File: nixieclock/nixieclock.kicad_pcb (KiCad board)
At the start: 4 copper layers, 96.5 x 92.8 mm, 136 parts, among them J1 USB_C_Receptacle, J2 Conn_ARM_JTAG_SWD_10, Q10 BSS131, Q11 BSS131, Q12 BSS131, Q13 BSS131, Q14 BSS131, Q15 BSS131, Q16 BSS131, Q17 BSS131, Q18 BSS131, Q19 BSS131, Q2 IRLR3110ZTRPBF, Q20 BSS131, Q21 BSS131, Q22 BSS131, Q23 BSS131, Q24 BSS131, Q25 BSS131, Q26 BSS131, Q27 BSS131, Q28 BSS131, Q29 BSS131, Q3 BSR92P, Q30 BSS131, Q31 BSS131, Q32 BSS131, Q33 BSS131, Q34 BSS131, Q35 BSS131, Q36 BSS131, Q37 BSS131, Q38 BSS131, Q39 BSS131, Q4 BSR92P, Q40 BSS131, Q41 BSS131, Q42 BSS131, Q43 BSS131, Q44 BSS131, Q45 BSS131, Q46 BSS131, Q47 BSS131, Q48 BSS131, Q5 BSS131, Q6 BSS131, Q7 BSS131, Q8 BSS131, Q9 BSS131, SW1 EN11-VSM, U1 LT3757AEMSE, U2 AMS1117-3.3, U3 74HC595, U4 74HC595, U5 74HC595, U6 74HC595, U7 74HC595, U8 STM32F051R4Tx, Y1 8MHz, Y2 32.768kHz

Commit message: finalized design ready for quality check
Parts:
- added D2: LTST-C190GKT, LED_SMD:LED_0603_1608Metric_Pad1.05x0.95mm_HandSolder, F.Cu at (113.0, 76.8)
- added D3: LTST-C190GKT, LED_SMD:LED_0603_1608Metric_Pad1.05x0.95mm_HandSolder, F.Cu at (114.8, 76.8)
- added D4: LTST-C190GKT, LED_SMD:LED_0603_1608Metric_Pad1.05x0.95mm_HandSolder, F.Cu at (116.5, 76.8)
- added H1: MountingHole, MountingHole:MountingHole_5.3mm_M5_Pad, F.Cu at (56.0, 76.0)
- added H2: MountingHole, MountingHole:MountingHole_5.3mm_M5_Pad, F.Cu at (56.0, 157.0)
- added H3: MountingHole, MountingHole:MountingHole_5.3mm_M5_Pad, F.Cu at (164.0, 157.0)
- added H4: MountingHole, MountingHole:MountingHole_5.3mm_M5_Pad, F.Cu at (164.0, 76.0)
- added R32: 3.3k, Resistor_SMD:R_0603_1608Metric_Pad1.05x0.95mm_HandSolder, F.Cu at (113.0, 80.2)
- added R33: 1.2k, Resistor_SMD:R_0603_1608Metric_Pad1.05x0.95mm_HandSolder, F.Cu at (114.8, 80.2)
- added R34: 1.2k, Resistor_SMD:R_0603_1608Metric_Pad1.05x0.95mm_HandSolder, F.Cu at (116.5, 80.2)
- added R35: 1M, Resistor_SMD:R_0603_1608Metric_Pad1.05x0.95mm_HandSolder, F.Cu at (72.5, 113.2)
- added R36: 1M, Resistor_SMD:R_0603_1608Metric_Pad1.05x0.95mm_HandSolder, F.Cu at (80.5, 113.2)
- added R37: 1M, Resistor_SMD:R_0603_1608Metric_Pad1.05x0.95mm_HandSolder, F.Cu at (84.5, 113.2)
- added R38: 1M, Resistor_SMD:R_0603_1608Metric_Pad1.05x0.95mm_HandSolder, F.Cu at (84.5, 139.3)
- added R39: 1M, Resistor_SMD:R_0603_1608Metric_Pad1.05x0.95mm_HandSolder, F.Cu at (82.3, 142.3)
- added R40: 1M, Resistor_SMD:R_0603_1608Metric_Pad1.05x0.95mm_HandSolder, F.Cu at (78.5, 146.3)
- added R41: 1M, Resistor_SMD:R_0603_1608Metric_Pad1.05x0.95mm_HandSolder, F.Cu at (74.5, 146.3)
- added R42: 1M, Resistor_SMD:R_0603_1608Metric_Pad1.05x0.95mm_HandSolder, F.Cu at (70.7, 142.3)
- added R43: 1M, Resistor_SMD:R_0603_1608Metric_Pad1.05x0.95mm_HandSolder, F.Cu at (68.5, 139.3)
- added R44: 1M, Resistor_SMD:R_0603_1608Metric_Pad1.05x0.95mm_HandSolder, F.Cu at (68.5, 113.2)
- added R45: 1M, Resistor_SMD:R_0603_1608Metric_Pad1.05x0.95mm_HandSolder, F.Cu at (92.5, 113.2)
- added R46: 1M, Resistor_SMD:R_0603_1608Metric_Pad1.05x0.95mm_HandSolder, F.Cu at (100.5, 113.2)
- added R47: 1M, Resistor_SMD:R_0603_1608Metric_Pad1.05x0.95mm_HandSolder, F.Cu at (104.5, 113.2)
- added R48: 1M, Resistor_SMD:R_0603_1608Metric_Pad1.05x0.95mm_HandSolder, F.Cu at (104.5, 139.3)
- added R49: 1M, Resistor_SMD:R_0603_1608Metric_Pad1.05x0.95mm_HandSolder, F.Cu at (102.3, 142.3)
- added R50: 1M, Resistor_SMD:R_0603_1608Metric_Pad1.05x0.95mm_HandSolder, F.Cu at (98.5, 146.3)
- added R51: 1M, Resistor_SMD:R_0603_1608Metric_Pad1.05x0.95mm_HandSolder, F.Cu at (94.5, 146.3)
- added R52: 1M, Resistor_SMD:R_0603_1608Metric_Pad1.05x0.95mm_HandSolder, F.Cu at (90.7, 142.3)
- added R53: 1M, Resistor_SMD:R_0603_1608Metric_Pad1.05x0.95mm_HandSolder, F.Cu at (88.5, 139.3)
- added R54: 1M, Resistor_SMD:R_0603_1608Metric_Pad1.05x0.95mm_HandSolder, F.Cu at (88.5, 113.2)
- added R55: 1M, Resistor_SMD:R_0603_1608Metric_Pad1.05x0.95mm_HandSolder, F.Cu at (119.5, 113.2)
- added R56: 1M, Resistor_SMD:R_0603_1608Metric_Pad1.05x0.95mm_HandSolder, F.Cu at (127.5, 113.2)
- added R57: 1M, Resistor_SMD:R_0603_1608Metric_Pad1.05x0.95mm_HandSolder, F.Cu at (131.5, 113.2)
- added R58: 1M, Resistor_SMD:R_0603_1608Metric_Pad1.05x0.95mm_HandSolder, F.Cu at (131.5, 139.3)
- added R59: 1M, Resistor_SMD:R_0603_1608Metric_Pad1.05x0.95mm_HandSolder, F.Cu at (129.3, 142.3)
- added R60: 1M, Resistor_SMD:R_0603_1608Metric_Pad1.05x0.95mm_HandSolder, F.Cu at (125.5, 146.3)
- added R61: 1M, Resistor_SMD:R_0603_1608Metric_Pad1.05x0.95mm_HandSolder, F.Cu at (121.5, 146.3)
- added R62: 1M, Resistor_SMD:R_0603_1608Metric_Pad1.05x0.95mm_HandSolder, F.Cu at (117.7, 142.3)
- added R63: 1M, Resistor_SMD:R_0603_1608Metric_Pad1.05x0.95mm_HandSolder, F.Cu at (115.5, 139.3)
- added R64: 1M, Resistor_SMD:R_0603_1608Metric_Pad1.05x0.95mm_HandSolder, F.Cu at (115.5, 113.2)
- added R65: 1M, Resistor_SMD:R_0603_1608Metric_Pad1.05x0.95mm_HandSolder, F.Cu at (139.5, 113.2)
- added R66: 1M, Resistor_SMD:R_0603_1608Metric_Pad1.05x0.95mm_HandSolder, F.Cu at (147.5, 113.2)
- added R67: 1M, Resistor_SMD:R_0603_1608Metric_Pad1.05x0.95mm_HandSolder, F.Cu at (151.5, 113.2)
- added R68: 1M, Resistor_SMD:R_0603_1608Metric_Pad1.05x0.95mm_HandSolder, F.Cu at (151.5, 139.3)
- added R69: 1M, Resistor_SMD:R_0603_1608Metric_Pad1.05x0.95mm_HandSolder, F.Cu at (149.3, 142.3)
- added R70: 1M, Resistor_SMD:R_0603_1608Metric_Pad1.05x0.95mm_HandSolder, F.Cu at (145.5, 146.3)
- added R71: 1M, Resistor_SMD:R_0603_1608Metric_Pad1.05x0.95mm_HandSolder, F.Cu at (141.5, 146.3)
- added R72: 1M, Resistor_SMD:R_0603_1608Metric_Pad1.05x0.95mm_HandSolder, F.Cu at (137.7, 142.3)
- added R73: 1M, Resistor_SMD:R_0603_1608Metric_Pad1.05x0.95mm_HandSolder, F.Cu at (135.5, 139.3)
- added R74: 1M, Resistor_SMD:R_0603_1608Metric_Pad1.05x0.95mm_HandSolder, F.Cu at (135.5, 113.2)
- BT1: footprint Battery:BatteryHolder_Keystone_3000_1x12mm -> Battery:BatteryHolder_MPD_BK912-1x2032
- R21, R22, R23, R24: value 10k -> ?
- R3: value 140k -> 10k
- moved G2 11.2 mm to (122.5, 92.2)
- moved R30 9.63 mm to (146.4, 81.5), turned to 180 degrees
- moved R31 9.19 mm to (144.2, 79.8), turned to 180 degrees
- moved C29 8.54 mm to (155.2, 83.2)
- moved C31 7.37 mm to (144.2, 83.2)
- moved R29 6.96 mm to (153.1, 81.5), turned to 180 degrees
- moved BT1 5.36 mm to (128.6, 79.8)
- moved R19 3.09 mm to (155.2, 79.8), turned to 180 degrees
- moved R20 2.51 mm to (149.8, 83.0)
- moved C30 1.87 mm to (149.8, 80.0)
- moved C1 1.25 mm to (78.5, 86.2)
- moved C10 1.25 mm to (68.2, 85.7)
- moved C11 1.25 mm to (72.0, 82.8)
- moved C12 1.25 mm to (73.5, 82.8)
- moved C13 1.25 mm to (98.0, 79.2)
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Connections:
- R3 pad 1: +3V3 -> GND
- SW1 pad A: (no net) -> Net-(R19-Pad2)
- SW1 pad B: (no net) -> Net-(R30-Pad2)
- U8 pad 37: (no net) -> /microcontroller/ENC_A
- U8 pad 38: (no net) -> /microcontroller/ENC_B
- U8 pad 39: (no net) -> /microcontroller/ENC_SW
- U8 pad 50: (no net) -> Net-(D4-Pad2)
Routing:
- net GND: track 222.3 -> 267.3 mm, vias 208 -> 158
- net Net-(D4-Pad2): track 0.00 -> 30.2 mm
- net /microcontroller/VBAT: track 50.0 -> 71.9 mm
- net VCC: track 16.8 -> 34.3 mm, vias 5 -> 7
- net /microcontroller/ENC_SW: track 0.00 -> 16.9 mm, vias 0 -> 2
- net +3V3: track 33.0 -> 49.5 mm, vias 21 -> 23
- net /cathode_registers/GB0: track 48.0 -> 64.2 mm
- net /microcontroller/ENC_A: track 0.00 -> 11.3 mm
- net Net-(R30-Pad2): track 0.00 -> 9.80 mm
- net Net-(R19-Pad2): track 0.00 -> 9.80 mm
- net /cathode_registers/GB8: track 39.2 -> 30.4 mm
- net /microcontroller/ENC_B: track 0.00 -> 7.62 mm
- net /cathode_registers/LCLK: track 179.5 -> 175.1 mm
- net /cathode_registers/~RES: track 158.2 -> 153.8 mm
- net /cathode_registers/~OE: track 186.2 -> 181.9 mm
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- added copper zone on F.Cu, net Net-(F1-Pad2)
- removed copper zone on F.Cu, net (none)
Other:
- board size 96.5 x 92.8 mm -> 120 x 93 mm
- board text added: "3.3V"
- board text added: "MCU"
- board text added: "VCC"

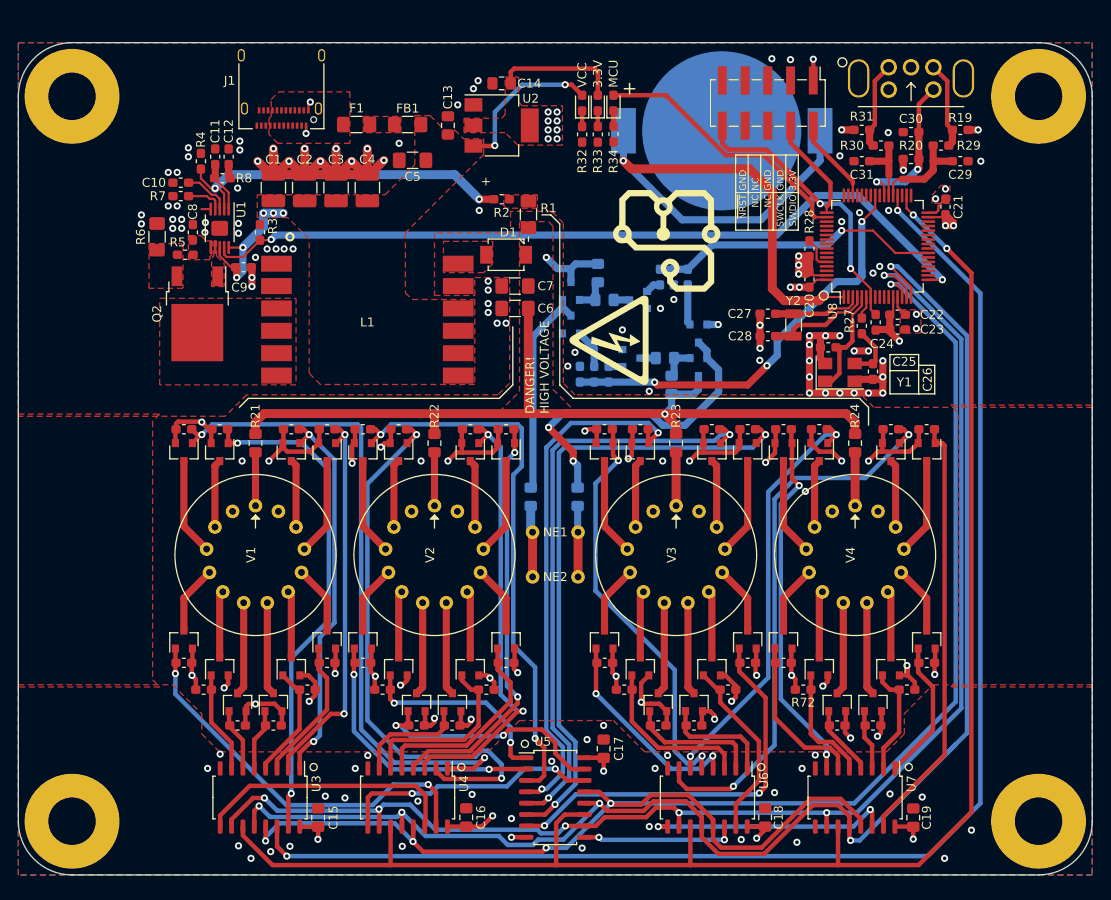
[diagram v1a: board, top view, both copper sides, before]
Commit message: finalized design, fixed USB C receptacle for hand soldering
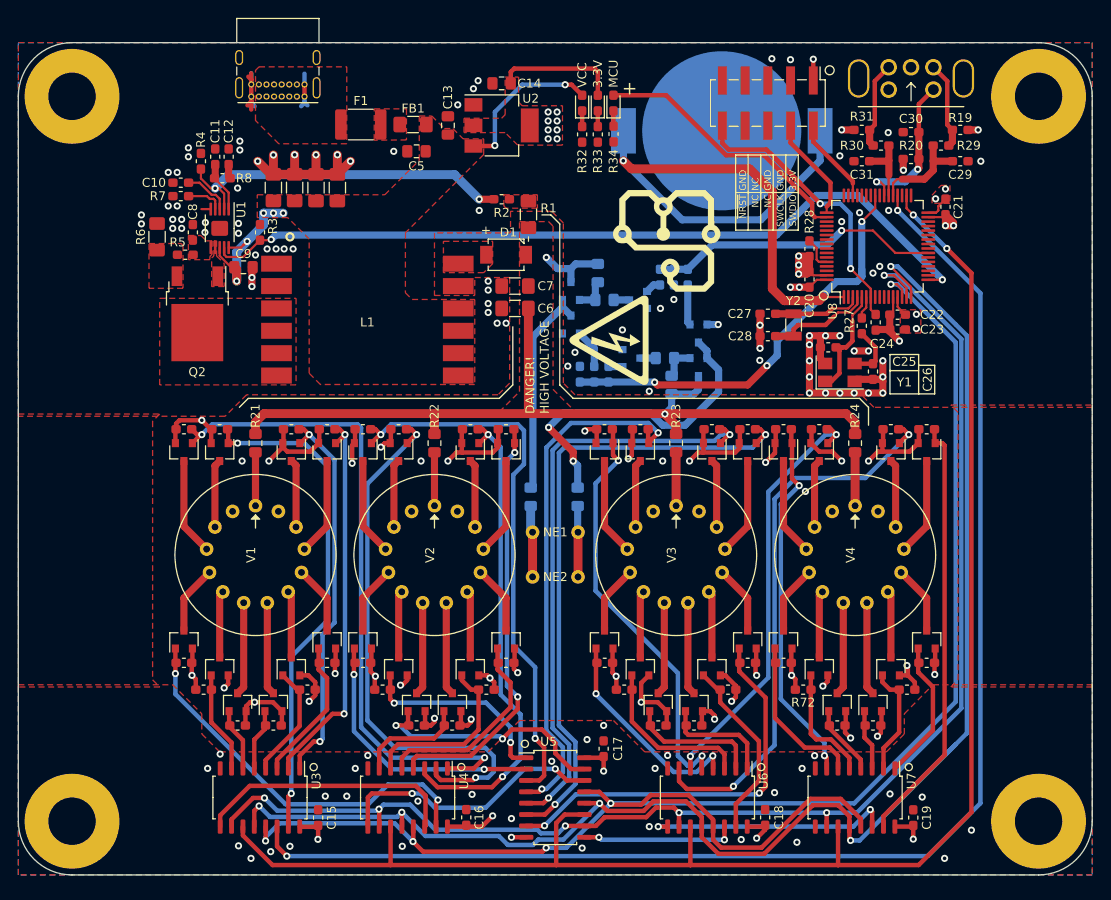
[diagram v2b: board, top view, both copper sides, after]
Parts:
- C1, C2, C3, C4: footprint Capacitor_SMD:C_1210_3225Metric_Pad1.42x2.65mm_HandSolder -> Capacitor_SMD:C_1206_3216Metric_Pad1.42x1.75mm_HandSolder
- C15, C16, C17, C18, C19: footprint Capacitor_SMD:C_0805_2012Metric_Pad1.15x1.40mm_HandSolder -> Capacitor_SMD:C_0603_1608Metric_Pad1.05x0.95mm_HandSolder
- C5: footprint Capacitor_SMD:C_1206_3216Metric_Pad1.42x1.75mm_HandSolder -> Capacitor_SMD:C_0805_2012Metric_Pad1.15x1.40mm_HandSolder
- C9: footprint Capacitor_SMD:C_0603_1608Metric_Pad1.05x0.95mm_HandSolder -> Capacitor_SMD:C_0805_2012Metric_Pad1.15x1.40mm_HandSolder
- F1: value 1A -> 2.2A; footprint Fuse:Fuse_1206_3216Metric_Pad1.42x1.75mm_HandSolder -> Fuse:Fuse_1812_4532Metric_Pad1.30x3.40mm_HandSolder
- FB1: value 600 @ 600MHz -> 100 @ 100MHz
- J1: value USB_C_Receptacle -> USB_C_Receptacle_USB2.0; footprint Connector_USB:USB_C_Receptacle_Amphenol_12401610E4-2A -> Connector_USB:USB_C_Receptacle_GCT_USB4085
- R15, R16: value R_Small -> 1M
- R2: value 64.4k -> 63.4k
- R21, R22, R23, R24: value ? -> 13k
- moved C4 3.35 mm to (85.6, 86.2)
- moved J1 3.13 mm to (82.0, 76.0)
- moved C3 2.24 mm to (83.3, 86.2)
- moved C2 1.13 mm to (80.9, 86.2)
- moved C5 1.10 mm to (94.5, 82.1)
- moved FB1 0.61 mm to (94.1, 79.2)
- moved F1 0.47 mm to (88.3, 79.2)
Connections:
- J1 pad A5: (no net) -> unconnected-(J1-PadA5)
- J1 pad A6: (no net) -> unconnected-(J1-PadA6)
- J1 pad A7: (no net) -> unconnected-(J1-PadA7)
- J1 pad A8: (no net) -> unconnected-(J1-PadA8)
- J1 pad B5: (no net) -> unconnected-(J1-PadB5)
- J1 pad B6: (no net) -> unconnected-(J1-PadB6)
- J1 pad B7: (no net) -> unconnected-(J1-PadB7)
- J1 pad B8: (no net) -> unconnected-(J1-PadB8)
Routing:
- net GND: track 267.3 -> 257.5 mm, vias 158 -> 153
- net /cathode_registers/GB1: track 49.1 -> 53.8 mm
- net VCC: track 34.3 -> 36.5 mm
- net /cathode_registers/GB0: track 64.2 -> 62.4 mm
- net Net-(U4-Pad9): track 29.3 -> 30.6 mm
- net /cathode_registers/GB2: track 46.4 -> 47.2 mm
- net /cathode_registers/GA9: track 75.2 -> 74.6 mm
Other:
- board text added: "JLCJLCJLCJLC"
- board text added: "Made with love for Clair, Happy Birthday"
